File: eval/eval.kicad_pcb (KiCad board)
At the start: 2 copper layers, 38 x 90.7 mm, 122 parts, among them J1 TC2030, Q1 BSC0702LS, Q2 BSC0702LS, Q3 AP40P04G, Q4 DMG2302UK-7, Q5 BSC0702LS, Q6 BSC0702LS, Q7 WSD4070DN, Q8 WSD4070DN, U1 AP63205WU-7, U10 TPS7A2033PDBVR, U11 RCLAMP0521T-ES, U12 TPS7A2033PDBVR, U13 RCLAMP0521T-ES, U14 TLV9061xDBV, U15 TCAN1044VDRBRQ1, U16 MX74700T_C22468156, U17 MX74700T_C22468156, U2 LM5148RGYR, U3 INA180A3, U4 HUSB238A-BB001-QN16R, U5 TLV9064, U6 HS096T01H13, U7 MX74502D23_C41433189, U8 INA180A3, U9 STM32G0B1CBTx

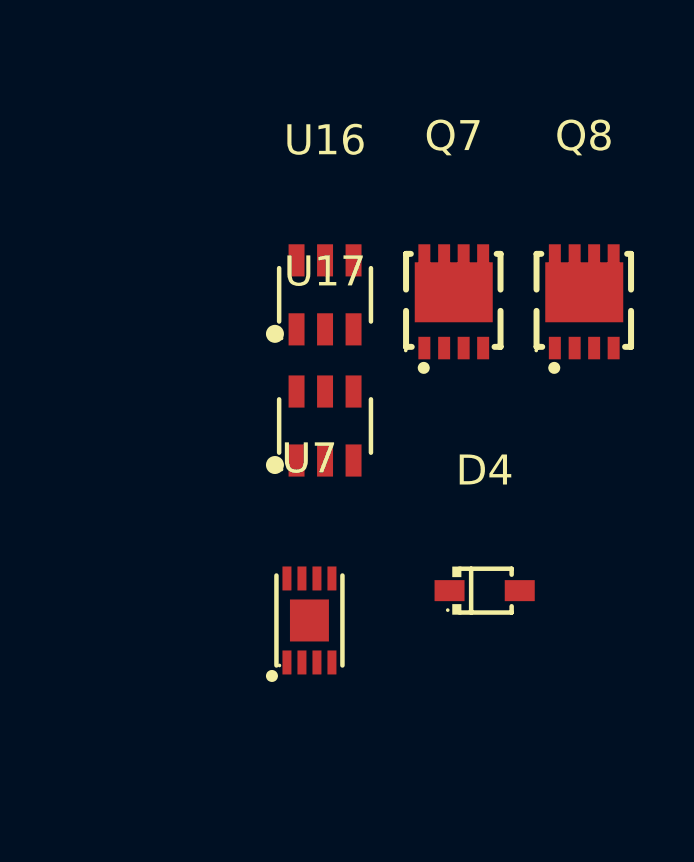
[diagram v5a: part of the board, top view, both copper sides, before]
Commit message: [sch]power_battery: add feature voltage drop, current rush, MCU input, reverse protection
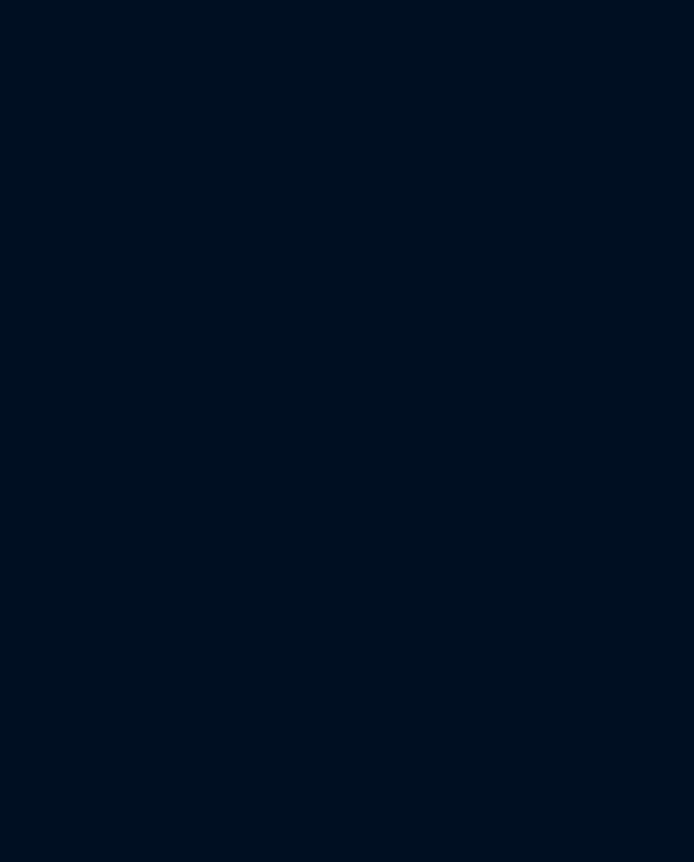
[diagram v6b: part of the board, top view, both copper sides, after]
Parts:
- removed D4: BZX384-C12,115, EasyEDA:SOD-323_L1.8-W1.3-LS2.5-RD
- removed Q7, Q8: WSD4070DN, EasyEDA:PDFN3333-8_L3.1-W3.2-P0.65-LS3.4-BL
- removed U16, U17: MX74700T_C22468156, EasyEDA:SOT-23-6_L2.9-W1.6-P0.95-LS2.9-BL
- removed U7: MX74502D23_C41433189, EasyEDA:UDFN-8L_L2.0-W3.0-P0.50-BL-EP

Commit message: [layout] first draft layout
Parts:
- added C47: 100n@40v, Capacitor_SMD:C_0603_1608Metric, F.Cu at (-17.9, 66.8)
- added C48: 100n@40v, Capacitor_SMD:C_0603_1608Metric, F.Cu at (-17.9, 69.4)
- added C49: C_Small, Capacitor_SMD:C_0603_1608Metric, F.Cu at (-31.2, 153.7)
- added C50: 100n, Capacitor_SMD:C_0603_1608Metric, F.Cu at (-79.1, 179.6)
- added C51: 1n, Capacitor_SMD:C_0603_1608Metric, F.Cu at (-88.7, 204.0)
- added C52: 10n, Capacitor_SMD:C_0603_1608Metric, F.Cu at (-88.8, 207.9)
- added C53: 47n, Capacitor_SMD:C_0603_1608Metric, F.Cu at (-78.2, 206.7)
- added C54: 100n, Capacitor_SMD:C_0603_1608Metric, F.Cu at (-85.7, 211.7)
- added C55: 1u, Capacitor_SMD:C_0603_1608Metric, F.Cu at (-85.7, 210.1)
- added C56: 100n, Capacitor_SMD:C_0603_1608Metric, F.Cu at (-87.3, 191.3)
- added C57: 100n, Capacitor_SMD:C_0603_1608Metric, F.Cu at (-80.8, 189.5)
- added C58: 1u, Capacitor_SMD:C_0603_1608Metric, F.Cu at (-84.0, 189.5)
- added C59: 1n, Capacitor_SMD:C_0603_1608Metric, F.Cu at (-87.3, 194.5)
- added C60: 4.7n, Capacitor_SMD:C_0603_1608Metric, F.Cu at (-77.4, 191.6)
- added C61: 1u, Capacitor_SMD:C_0603_1608Metric, F.Cu at (-51.0, 133.0)
- added D4: BZX384-C12,115, EasyEDA:SOD-323_L1.8-W1.3-LS2.5-RD, F.Cu at (88.5, 75.3)
- added D5: BAT54,215, EasyEDA:SOT-23_L2.9-W1.3-P1.90-LS2.4-BR, F.Cu at (-74.5, 207.1)
- added Q10: 2N7002, Package_TO_SOT_SMD:SOT-23, F.Cu at (-46.2, 132.9)
- added Q7: WSD4070DN, EasyEDA:PDFN3333-8_L3.1-W3.2-P0.65-LS3.4-BL, F.Cu at (-3.96, 67.9)
- added Q8: WSD4070DN, EasyEDA:PDFN3333-8_L3.1-W3.2-P0.65-LS3.4-BL, F.Cu at (0.39, 67.9)
- added Q9: 2N7002, Package_TO_SOT_SMD:SOT-23, F.Cu at (-46.5, 144.9)
- added R16: 10k, Resistor_SMD:R_0603_1608Metric, F.Cu at (-92.0, 204.0)
- added R19: 10k, Resistor_SMD:R_0603_1608Metric, F.Cu at (-90.4, 203.9)
- added R25: 22k, Resistor_SMD:R_0603_1608Metric, F.Cu at (-92.1, 207.9)
- added R48: 15k, Resistor_SMD:R_0603_1608Metric, F.Cu at (-90.4, 207.9)
- added R49: 100, Resistor_SMD:R_0603_1608Metric, F.Cu at (-78.3, 208.3)
- added R50: 500k, Resistor_SMD:R_0603_1608Metric, F.Cu at (-78.3, 205.1)
- added R51: 30.1k, Resistor_SMD:R_0603_1608Metric, F.Cu at (-90.5, 194.4)
- added R52: 59k, Resistor_SMD:R_0603_1608Metric, F.Cu at (-88.9, 194.4)
- added R53: 20k, Resistor_SMD:R_0603_1608Metric, F.Cu at (-92.9, 193.7)
- added R54: 15k, Resistor_SMD:R_0603_1608Metric, F.Cu at (-90.6, 191.2)
- added R55: 10k, Resistor_SMD:R_0603_1608Metric, F.Cu at (-88.9, 191.2)
- added R56: 100, Resistor_SMD:R_0603_1608Metric, F.Cu at (-50.2, 146.1)
- added R58: 1k, Resistor_SMD:R_0603_1608Metric, F.Cu at (-59.5, 158.7)
- added R59: 8.06k, Resistor_SMD:R_0603_1608Metric, F.Cu at (-75.7, 194.9)
- added R60: 24.9k, Resistor_SMD:R_0603_1608Metric, F.Cu at (-77.4, 194.9)
- added R61: 4.7k, Resistor_SMD:R_0603_1608Metric, F.Cu at (-75.7, 191.7)
- added R64: 100k, Resistor_SMD:R_0603_1608Metric, F.Cu at (-49.4, 132.9)
- added R65: 1k, Resistor_SMD:R_0603_1608Metric, F.Cu at (-57.2, 145.1)
- added U16: MX74700T_C22468156, EasyEDA:SOT-23-6_L2.9-W1.6-P0.95-LS2.9-BL, F.Cu at (-8.25, 67.7)
- added U17: MX74700T_C22468156, EasyEDA:SOT-23-6_L2.9-W1.6-P0.95-LS2.9-BL, F.Cu at (-8.25, 72.1)
- added U20: TLV3501AIDBV, Package_SO:SOIC-8_3.9x4.9mm_P1.27mm, F.Cu at (-83.8, 206.4)
- added U21: LM2901, Package_SO:TSSOP-14_4.4x5mm_P0.65mm, F.Cu at (-82.3, 193.1)
- added U22: SN74LVC1G00DBV, Package_TO_SOT_SMD:SOT-23-5, F.Cu at (-54.0, 145.2)
- added U23: SN74LVC1G00DBV, Package_TO_SOT_SMD:SOT-23-5, F.Cu at (-54.0, 148.8)
- added U24: HYG015N03LS1C2, EasyEDA:PDFN-8_L5.9-W5.2-P1.27-LS6.2-BL, F.Cu at (61.3, 149.7)
- added U25: HYG015N03LS1C2, EasyEDA:PDFN-8_L5.9-W5.2-P1.27-LS6.2-BL, F.Cu at (52.7, 149.7)
- added U7: MX74502D23_C41433189, EasyEDA:UDFN-8L_L2.0-W3.0-P0.50-BL-EP, F.Cu at (-25.4, 153.8)
- moved D5 43.4 mm to (34.0, 43.9)
- moved L1 31.8 mm to (95.0, 124.8), turned to 180 degrees
- moved C6 28.4 mm to (77.3, 104.2), turned to 0 degrees
- moved C25 26.1 mm to (77.3, 105.9), turned to 0 degrees
- moved C45 24.3 mm to (77.3, 112.7), turned to 0 degrees
- moved C46 23.0 mm to (77.3, 114.4), turned to 0 degrees
- moved C43 22.1 mm to (78.5, 123.6), turned to 0 degrees
- moved C40 22.0 mm to (78.5, 121.0), turned to 0 degrees
- moved Q1 21.4 mm to (71.6, 105.5), turned to 90 degrees
- moved R45 19.6 mm to (60.4, 127.8)
- moved C39 19.1 mm to (60.5, 122.9)
- moved C9 17.1 mm to (78.5, 101.8), turned to 180 degrees
- moved C42 16.5 mm to (78.5, 126.8), turned to 0 degrees
- moved Q6 16.1 mm to (71.6, 113.5), turned to 90 degrees
- moved Q2 15.8 mm to (62.7, 105.5), turned to 90 degrees
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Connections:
- net /power/FB renamed /power_buck/FB
- net /power/IN_ISNS- renamed /power_buck/IN_ISNS-
- net /power/OUT_ISNS+ renamed /power_buck/OUT_ISNS+
- net /power/OUT_ISNS- renamed /power_buck/OUT_ISNS-
- net /power/PG/SYNCOUT renamed /power_buck/PG/SYNCOUT
- net /power/SW renamed /power_buck/SW
- net /power_mux/INPUT_A renamed /power_mux(page 10)/INPUT_A
- net /usb_pd/DEBUG renamed /power_usb_pd (page 9)/DEBUG
- net /usb_pd/FAULT renamed /power_usb_pd (page 9)/FAULT
- net /usb_pd/INT renamed /power_usb_pd (page 9)/INT
- net /usb_pd/ORIENT renamed /power_usb_pd (page 9)/ORIENT
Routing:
- net /power_battery/v_drop_fast: track 0.00 -> 5.88 mm
- net /power_battery/v_drop_slow: track 0.00 -> 5.84 mm
- net +3V3: track 13.1 -> 18.5 mm, vias 2 -> 4
- net /power_battery/fault_latch: track 0.00 -> 4.65 mm
- net Net-(U22-Pad2): track 0.00 -> 3.70 mm
- net Net-(R49-Pad1): track 0.00 -> 2.22 mm
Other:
- board size 38 x 90.7 mm -> 49.2 x 98 mm

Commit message: [layout] 50*100mm, without trace
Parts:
- removed the D5 at (-74.5, 207.1)
- removed the D5 at (34.0, 43.9)
- removed D6: SMAJ20A_C41376408, EasyEDA:SMA_L4.3-W2.6-LS5.2-RD
- removed R17, R20: 100, Resistor_SMD:R_0603_1608Metric
- removed U21: LM2901, Package_SO:TSSOP-14_4.4x5mm_P0.65mm
- removed U5: TLV9064, Package_SO:TSSOP-14_4.4x5mm_P0.65mm
- added CN1: XT30PW-M, EasyEDA:CONN-TH_XT30PW-M, F.Cu at (76.3, 66.0)
- added D5: BAT54J, Diode_SMD:D_SOD-323F, F.Cu at (70.1, 150.3)
- added D7: PTVSHC1SF24VBH, EasyEDA:SOD-123FL_L2.8-W1.8-LS3.7-BI, F.Cu at (67.4, 68.2)
- added R66: 1k, Resistor_SMD:R_0603_1608Metric, F.Cu at (77.0, 143.9)
- added U18: TLV3501AIDBV, Package_TO_SOT_SMD:SOT-23-6, F.Cu at (67.4, 146.5)
- added U19: TLV9062, Package_SO:TSSOP-8_4.4x3mm_P0.65mm, F.Cu at (38.7, 130.2)
- D1: value BAT54,215 -> BAT54J; footprint EasyEDA:SOT-23_L2.9-W1.3-P1.90-LS2.4-BR -> Diode_SMD:D_SOD-323F
- Q3: value AP40P04G -> AP40P04Q; footprint EasyEDA:PDFN-8_L5.8-W4.9-P1.27-LS6.1-BL-A -> EasyEDA:PDFN-8_L3.1-W3.0-P0.65-LS3.3-BL
- U20: value TLV3501AIDBV -> LM2903; footprint Package_SO:SOIC-8_3.9x4.9mm_P1.27mm -> Package_SO:TSSOP-8_4.4x3mm_P0.65mm
- moved R16 173.6 mm to (69.2, 139.7), turned to 180 degrees
- moved R25 171.9 mm to (65.7, 139.7), turned to 0 degrees
- moved R19 171.5 mm to (69.2, 141.4), turned to 0 degrees
- moved R48 169.7 mm to (65.7, 141.4), turned to 180 degrees
- moved C51 169.3 mm to (69.2, 143.1), turned to 0 degrees
- moved C52 167.5 mm to (65.7, 143.0), turned to 180 degrees
- moved C54 164.5 mm to (64.9, 145.4), turned to -90 degrees
- moved C55 162.7 mm to (64.9, 148.4), turned to -90 degrees
- moved R51 158.3 mm to (62.1, 152.5), turned to 180 degrees
- moved U20 157.7 mm to (61.2, 144.6), turned to 90 degrees
- moved R49 157.2 mm to (67.4, 149.5)
- moved R52 157.2 mm to (62.1, 150.8), turned to 0 degrees
- moved C59 156.1 mm to (62.1, 149.2), turned to 0 degrees
- moved C53 156.0 mm to (67.4, 151.0)
- moved R53 155.2 mm to (56.6, 151.7), turned to -90 degrees
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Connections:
- net /power_mux(page 10)/INPUT_A renamed /power_mux/INPUT_A
- net /power_mux(page 10)/INPUT_B renamed /power_dc_in/VDC
- net /power_usb_pd (page 9)/DEBUG renamed /power_usb_pd/DEBUG
- net /power_usb_pd (page 9)/FAULT renamed /power_usb_pd/FAULT
- net /power_usb_pd (page 9)/INT renamed /power_usb_pd/INT
- net /power_usb_pd (page 9)/ORIENT renamed /power_usb_pd/ORIENT
- net Net-(U5C-+) renamed /loop/V_CTL_FILT
- net Net-(U5D-+) renamed /loop/I_CTL_FILT
- C1 pad 2: /power_buck/SW -> Net-(U2-SW)
- C11 pad 2: Net-(D1-C) -> Net-(D1-K)
- D1 pad 1: Net-(D1-A) -> Net-(D1-K)
- D1 pad 2: unconnected-(D1-NC-Pad2) -> Net-(D1-A)
- Q1 pad 1: /power_buck/IN_ISNS- -> /power_buck/SW
- Q1 pad 2: /power_buck/IN_ISNS- -> /power_buck/SW
- Q1 pad 3: /power_buck/IN_ISNS- -> /power_buck/SW
- Q1 pad 5: /power_buck/SW -> /power_buck/IN_ISNS-
- Q1 pad 6: /power_buck/SW -> /power_buck/IN_ISNS-
- Q1 pad 7: /power_buck/SW -> /power_buck/IN_ISNS-
- Q1 pad 8: /power_buck/SW -> /power_buck/IN_ISNS-
- Q2 pad 1: /power_buck/SW -> GNDPWR
- Q2 pad 2: /power_buck/SW -> GNDPWR
- Q2 pad 3: /power_buck/SW -> GNDPWR
- Q2 pad 5: GNDPWR -> /power_buck/SW
- Q2 pad 6: GNDPWR -> /power_buck/SW
- Q2 pad 7: GNDPWR -> /power_buck/SW
- Q2 pad 8: GNDPWR -> /power_buck/SW
- Q5 pad 1: /power_buck/SW -> GNDPWR
- Q5 pad 2: /power_buck/SW -> GNDPWR
- Q5 pad 3: /power_buck/SW -> GNDPWR
- Q5 pad 5: GNDPWR -> /power_buck/SW
- Q5 pad 6: GNDPWR -> /power_buck/SW
- Q5 pad 7: GNDPWR -> /power_buck/SW
- Q5 pad 8: GNDPWR -> /power_buck/SW
- Q6 pad 1: /power_buck/IN_ISNS- -> /power_buck/SW
- Q6 pad 2: /power_buck/IN_ISNS- -> /power_buck/SW
- Q6 pad 3: /power_buck/IN_ISNS- -> /power_buck/SW
- Q6 pad 5: /power_buck/SW -> /power_buck/IN_ISNS-
- Q6 pad 6: /power_buck/SW -> /power_buck/IN_ISNS-
- Q6 pad 7: /power_buck/SW -> /power_buck/IN_ISNS-
- Q6 pad 8: /power_buck/SW -> /power_buck/IN_ISNS-
- R12 pad 1: Net-(D1-C) -> Net-(D1-K)
- U2 pad 14: /power_buck/SW -> Net-(U2-SW)
- U20 pad 1: /power_battery/v_drop_fast -> /power_battery/power_on_hold
- U20 pad 2: GNDA -> /power_battery/vbat_comp_thre
- U20 pad 3: /power_battery/v_drop_slow -> /power_battery/vbat_none_neg
- U20 pad 4: +3V3 -> GNDA
- U20 pad 5: Net-(R49-Pad1) -> /power_battery/i_mon_filter
- U20 pad 6: GNDA -> /power_battery/2v5
- U20 pad 7: (no net) -> /power_battery/power_on_hold
- U20 pad 8: (no net) -> +3V3
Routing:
- net Net-(Q2-G): track 0.00 -> 20.5 mm, vias 0 -> 3
- net Net-(Q1-G): track 0.00 -> 17.4 mm, vias 0 -> 3
- net +3V3: track 18.5 -> 10.3 mm, vias 4 -> 0
- net /power_buck/IN_ISNS-: track 0.00 -> 7.88 mm
- net Net-(D4-K): track 0.00 -> 7.79 mm
- net Net-(D3-C): track 0.00 -> 5.78 mm
- net /loop/I_CTL_BUFF: track 5.55 -> 0.00 mm
- net /loop/V_CTL_BUFF: track 5.45 -> 0.00 mm
- net /power_buck/FB: track 0.00 -> 5.31 mm
- net Net-(D4-A): track 0.00 -> 5.23 mm
- net Net-(U19A--): track 5.10 -> 0.00 mm
- net /loop/V_CTL_FILT: track 4.62 -> 0.00 mm
- net Net-(D2-C): track 0.00 -> 4.60 mm
- net /loop/I_CTL_FILT: track 4.45 -> 0.00 mm
- net Net-(D1-C): track 3.97 -> 0.00 mm
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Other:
- copper layers 2 -> 4
